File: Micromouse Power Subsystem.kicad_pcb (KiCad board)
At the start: 2 copper layers, 1 part, among them U1 INA219AxDCN

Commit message: Created branch for Josh
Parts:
- added J2: Conn_02x16_Odd_Even, Connector_PinHeader_2.54mm:PinHeader_2x16_P2.54mm_Vertical, F.Cu at (55.9, 63.5)
- added R1: 100m, Resistor_SMD:R_Shunt_Ohmite_LVK12, F.Cu at (62.8, 70.7)
- U1: value INA219AxDCN -> INA219AxD; footprint Package_TO_SOT_SMD:SOT-23-8 -> Package_SO:SOIC-8_3.9x4.9mm_P1.27mm
- moved U1 16.6 mm to (65.0, 64.4)
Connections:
- U1 pad 1: unconnected-(U1-IN+-Pad1) -> /3V3_OUT
- U1 pad 2: unconnected-(U1-IN--Pad2) -> GND
- U1 pad 3: unconnected-(U1-GND-Pad3) -> /SDA
- U1 pad 4: unconnected-(U1-VS-Pad4) -> /SCL
- U1 pad 5: unconnected-(U1-SCL-Pad5) -> /3V3_OUT
- U1 pad 6: unconnected-(U1-SDA-Pad6) -> GND
- U1 pad 7: unconnected-(U1-A0-Pad7) -> GND
- U1 pad 8: unconnected-(U1-A1-Pad8) -> /V_Switch

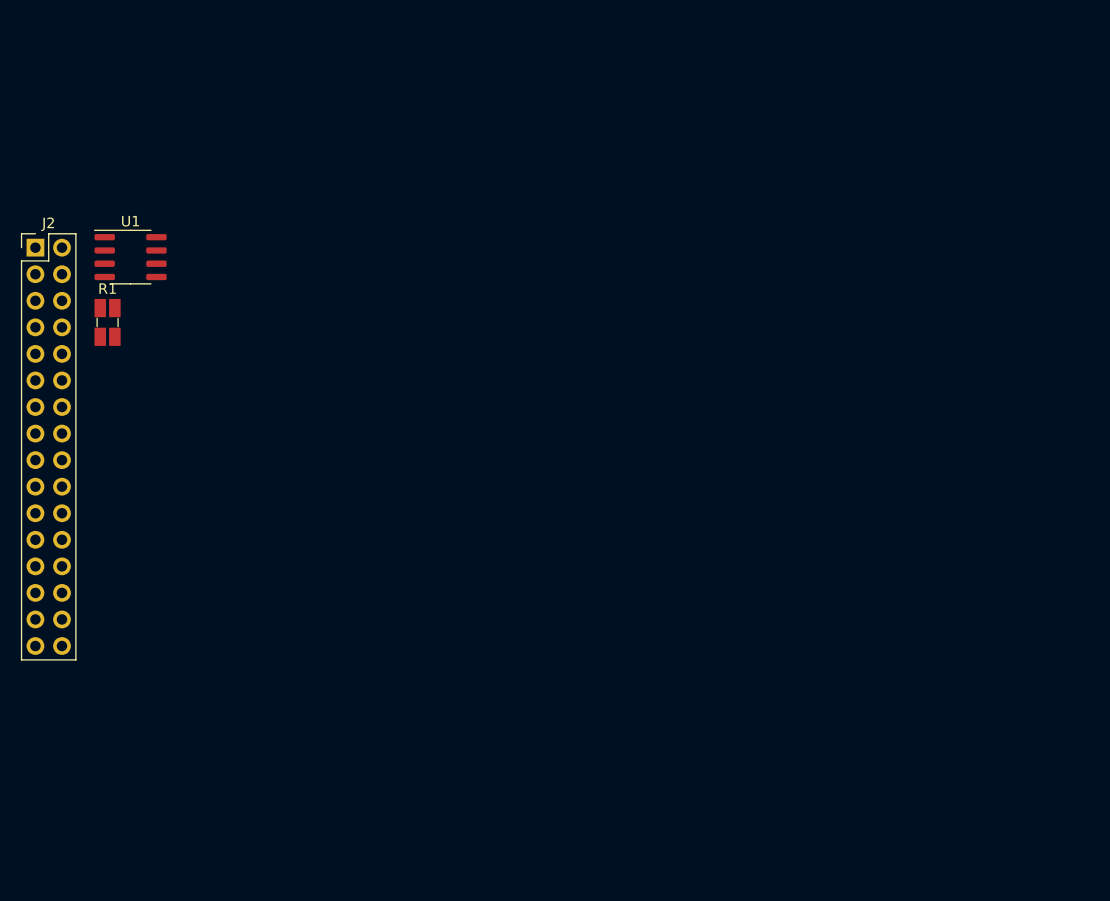
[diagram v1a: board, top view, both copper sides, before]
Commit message: Finished the USB-C integration with PD (9V)
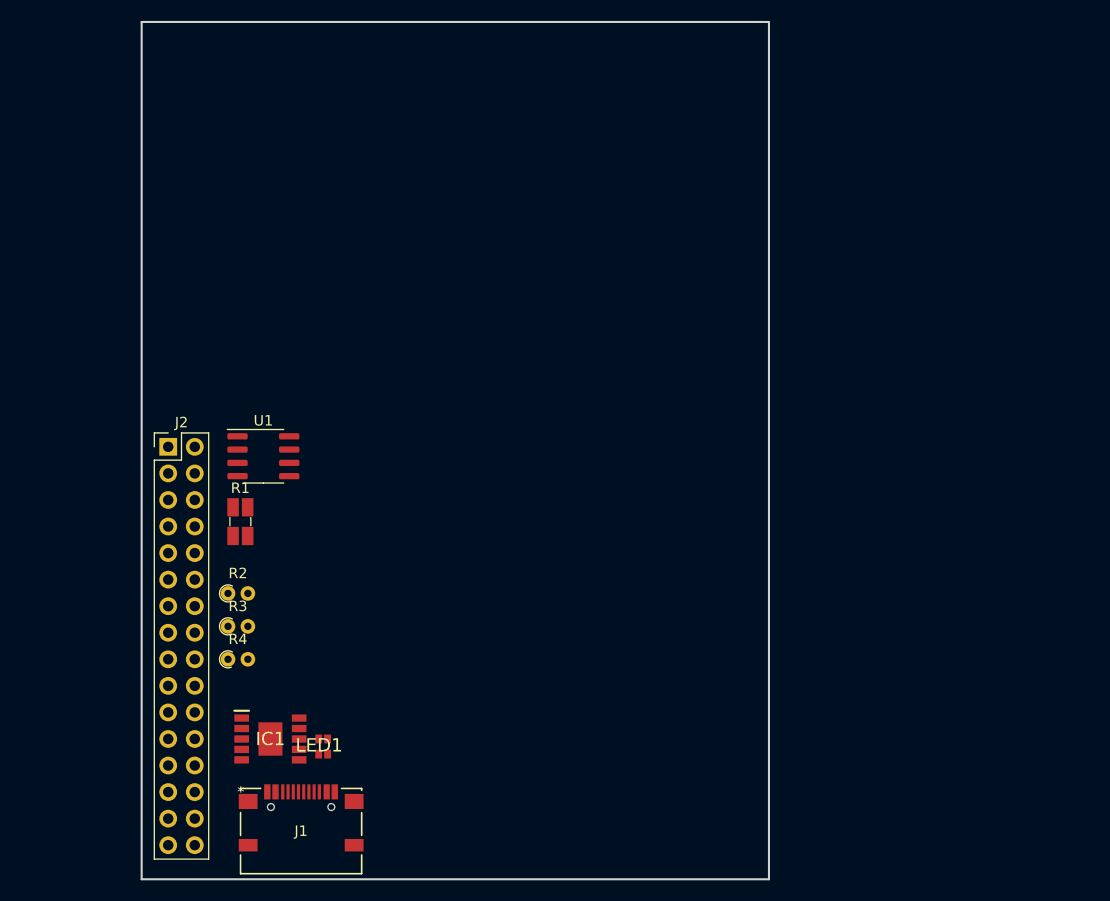
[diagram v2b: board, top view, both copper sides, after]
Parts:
- added IC1: CH224K, Components:SOP100P600X180-11N, F.Cu at (78.4, 110.5)
- added J1: TYPEC-304-ACP16, Components:TYPEC-304-ACP16_XNP, F.Cu at (81.3, 119.3)
- added LED1: LTST-C19HE1WT, RGB LED:LTST-C19HE1WT, F.Cu at (83.4, 111.2)
- added R2: 6.8k, Resistor_THT:R_Axial_DIN0204_L3.6mm_D1.6mm_P1.90mm_Vertical, F.Cu at (74.3, 96.6)
- added R3: 150R, Resistor_THT:R_Axial_DIN0204_L3.6mm_D1.6mm_P1.90mm_Vertical, F.Cu at (74.3, 99.7)
- added R4: 10k, Resistor_THT:R_Axial_DIN0204_L3.6mm_D1.6mm_P1.90mm_Vertical, F.Cu at (74.3, 102.9)
- U1: value INA219AxD -> INA219AIDCNR
- moved R1 22.9 mm to (75.5, 89.7)
- moved U1 22.9 mm to (77.7, 83.5)
- moved J2 22.9 mm to (68.6, 82.5)
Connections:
- J2 pad 1: unconnected-(J2-Pin_1-Pad1) -> /Motor2_B_OUT
- J2 pad 10: unconnected-(J2-Pin_10-Pad10) -> /Motor2_B_OUT
- J2 pad 11: unconnected-(J2-Pin_11-Pad11) -> /EXT_LOAD2_OUT
- J2 pad 12: unconnected-(J2-Pin_12-Pad12) -> /USART2_TX
- J2 pad 13: unconnected-(J2-Pin_13-Pad13) -> /FAST_CHARGE_CTRL
- J2 pad 18: /3V3_OUT -> +3V3
- J2 pad 2: unconnected-(J2-Pin_2-Pad2) -> /Motor2_A_OUT
- J2 pad 20: unconnected-(J2-Pin_20-Pad20) -> +5V
- J2 pad 21: unconnected-(J2-Pin_21-Pad21) -> /EXT_LOAD1_OUT
- J2 pad 22: unconnected-(J2-Pin_22-Pad22) -> /HV
- J2 pad 23: unconnected-(J2-Pin_23-Pad23) -> GND
- J2 pad 24: unconnected-(J2-Pin_24-Pad24) -> /MOTOR3_CTRL1
- J2 pad 25: unconnected-(J2-Pin_25-Pad25) -> /CTRL_EXT_LOAD1
- J2 pad 26: unconnected-(J2-Pin_26-Pad26) -> /MOTOR3_CTRL2
- J2 pad 27: unconnected-(J2-Pin_27-Pad27) -> /MOTOR3_A_OUT
- J2 pad 28: unconnected-(J2-Pin_28-Pad28) -> /MOTOR1_CTRL1
- J2 pad 29: unconnected-(J2-Pin_29-Pad29) -> /MOTOR3_B_OUT
- J2 pad 3: unconnected-(J2-Pin_3-Pad3) -> /Motor4_A_OUT
- J2 pad 30: unconnected-(J2-Pin_30-Pad30) -> /MOTOR1_CTRL2
- J2 pad 31: unconnected-(J2-Pin_31-Pad31) -> /MOTOR1_B_OUT
- J2 pad 32: unconnected-(J2-Pin_32-Pad32) -> /MOTOR1_A_OUT
- J2 pad 4: unconnected-(J2-Pin_4-Pad4) -> /Motor2_CTRL1
- J2 pad 5: unconnected-(J2-Pin_5-Pad5) -> /Motor4_B_OUT
- J2 pad 6: unconnected-(J2-Pin_6-Pad6) -> /Motor2_CTRL2
- J2 pad 7: unconnected-(J2-Pin_7-Pad7) -> /CTRL_EXT_LOAD2
- J2 pad 8: unconnected-(J2-Pin_8-Pad8) -> /Motor4_CTRL1
- J2 pad 9: unconnected-(J2-Pin_9-Pad9) -> /USART2_RX
- R1 pad 2: /V_Switch -> /BAT+
- U1 pad 1: /3V3_OUT -> /BAT+
- U1 pad 3: /SDA -> GND
- U1 pad 4: /SCL -> +3V3
- U1 pad 5: /3V3_OUT -> /SCL
- U1 pad 6: GND -> /SDA
- U1 pad 8: /V_Switch -> +3V3
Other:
- board outline added: 60 x 82 mm

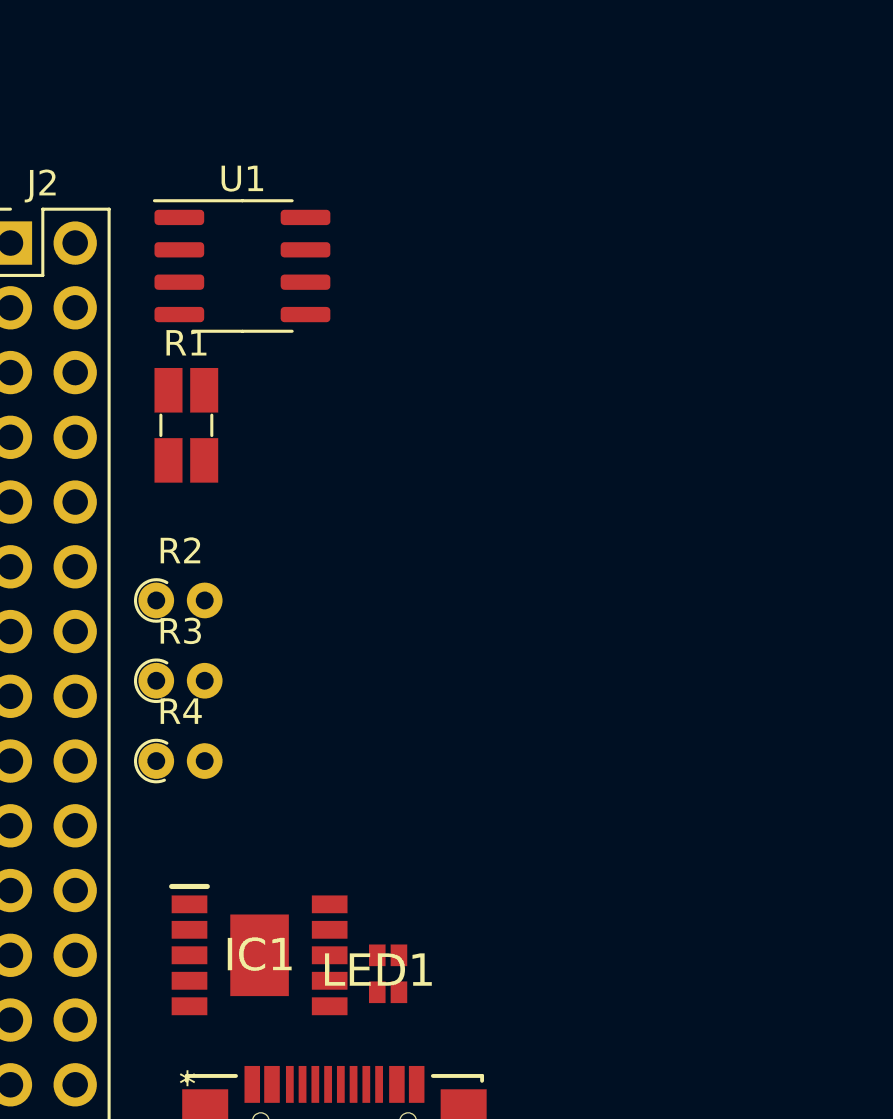
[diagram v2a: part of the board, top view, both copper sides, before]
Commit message: Added the charging modes as well as the charger powering the circuit when plugged in.
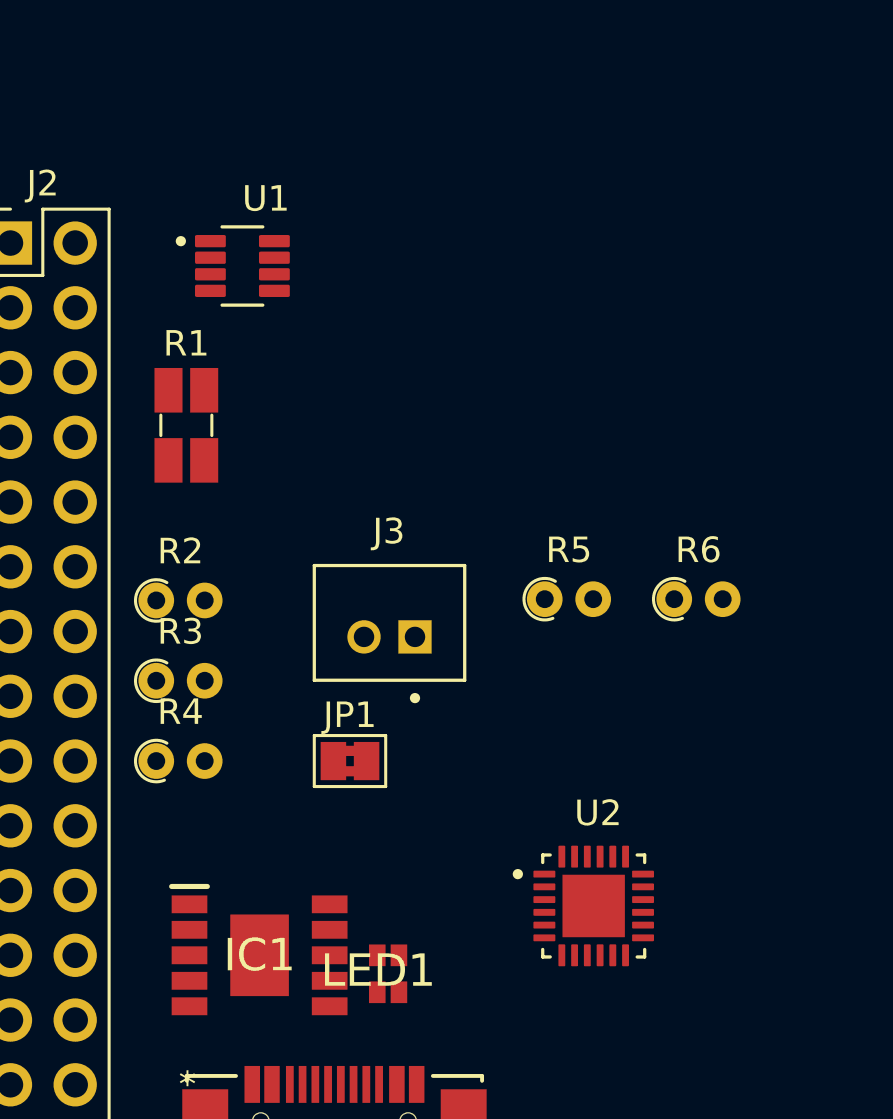
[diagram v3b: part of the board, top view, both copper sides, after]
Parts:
- added J3: B2B-PH-K-S, Battery JST Connector:JST_B2B-PH-K-S, F.Cu at (83.5, 97.5)
- added JP1: Jumper_2_Bridged, Jumper:SolderJumper-2_P1.3mm_Bridged2Bar_Pad1.0x1.5mm, F.Cu at (81.9, 102.9)
- added R5: 10k, Resistor_THT:R_Axial_DIN0204_L3.6mm_D1.6mm_P1.90mm_Vertical, F.Cu at (89.5, 96.5)
- added R6: 10k, Resistor_THT:R_Axial_DIN0204_L3.6mm_D1.6mm_P1.90mm_Vertical, F.Cu at (94.6, 96.5)
- added U2: BQ24610RGER, Battery Charger:QFN50P400X400X100-25N, F.Cu at (91.5, 108.6)
- U1: footprint Package_SO:SOIC-8_3.9x4.9mm_P1.27mm -> INA219:SOT65P280X145-8N

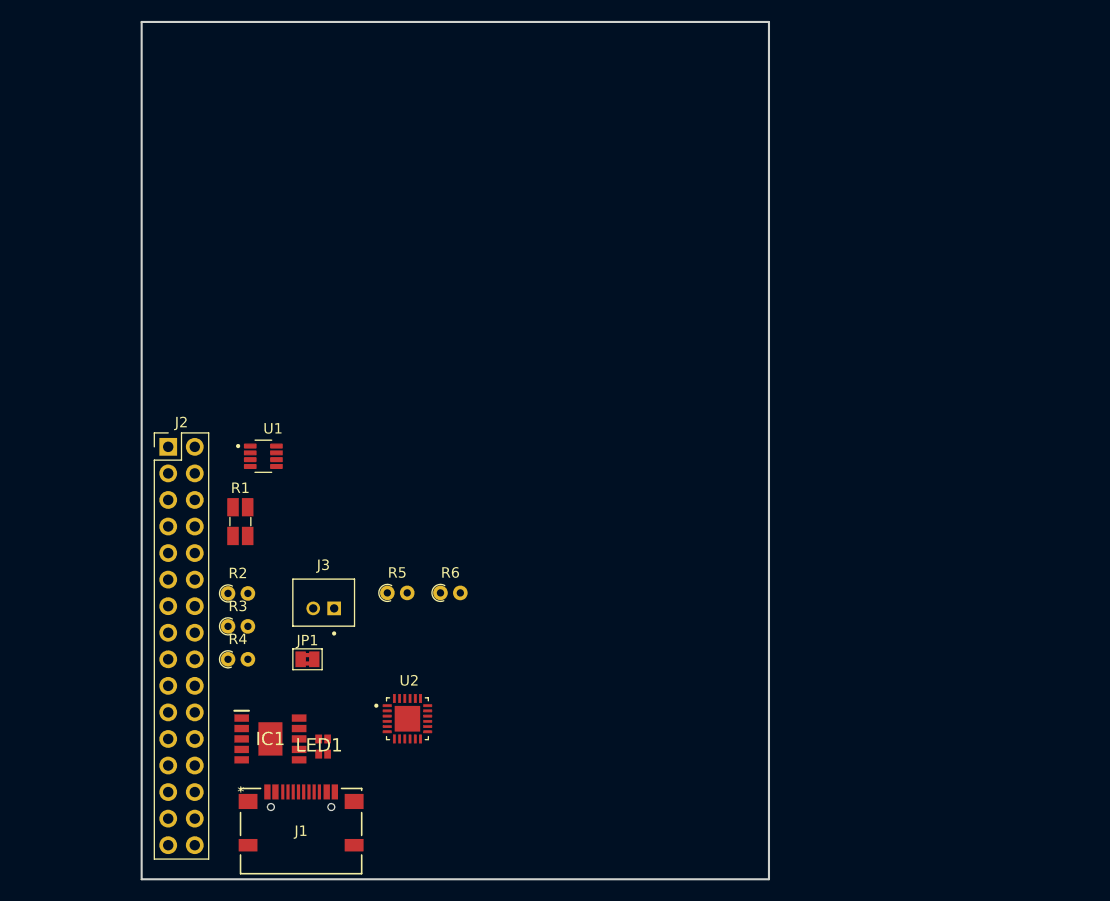
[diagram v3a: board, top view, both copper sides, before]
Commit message: Added completed schematic for my sections
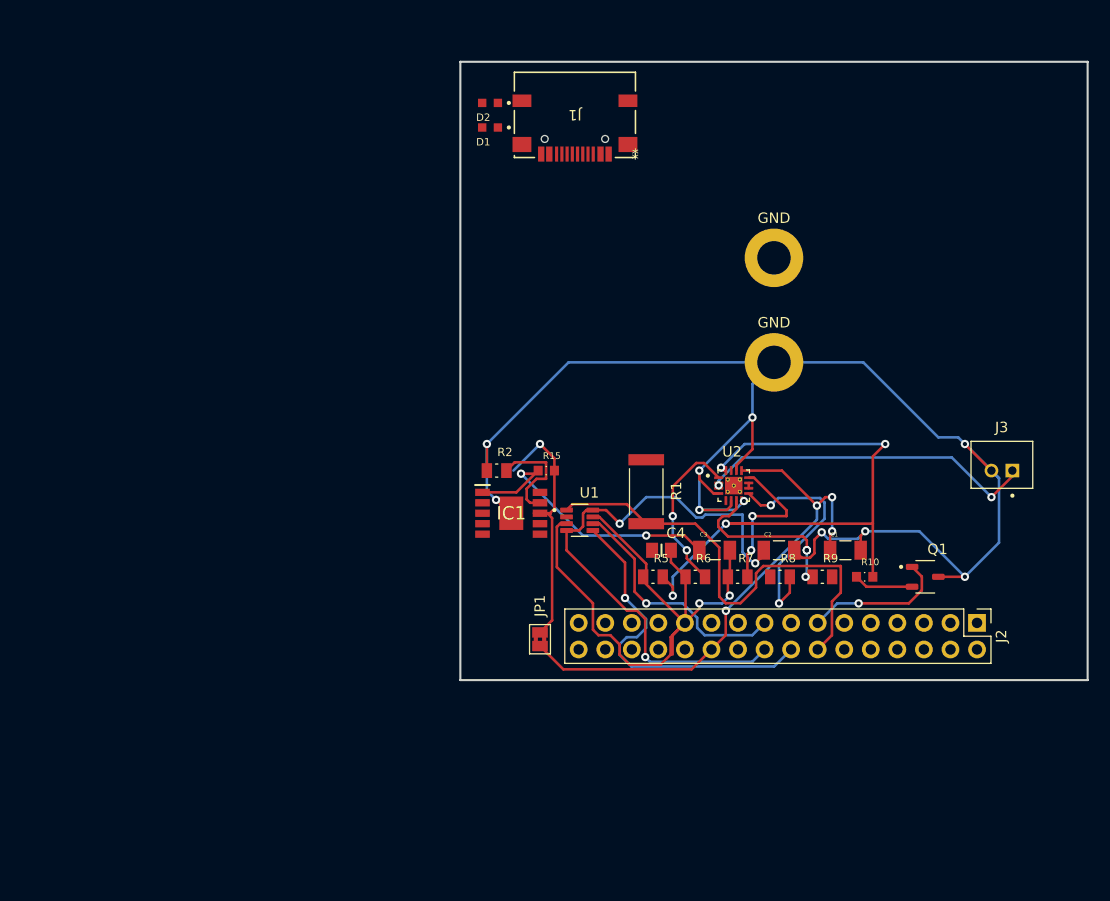
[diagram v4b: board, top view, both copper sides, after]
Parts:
- removed LED1: LTST-C19HE1WT, RGB LED:LTST-C19HE1WT
- removed R3: 150R, Resistor_THT:R_Axial_DIN0204_L3.6mm_D1.6mm_P1.90mm_Vertical
- removed R4: 10k, Resistor_THT:R_Axial_DIN0204_L3.6mm_D1.6mm_P1.90mm_Vertical
- added C1: 1µ, 1 micro:CAPC3216X180N, F.Cu at (133.3, 92.4)
- added C2: 10µ, 10 micro:CAPC3216X180N, F.Cu at (127.0, 92.4)
- added C3: 10µ, 10 micro:CAPC3216X180N, F.Cu at (120.8, 92.4)
- added C4: 4.7µ, 4.7 micro:CAPC2012X140N, F.Cu at (115.8, 92.4)
- added D1: KT-0805G (GREEN), LED:LED_KT-0603R, F.Cu at (99.4, 52.0)
- added D2: KT-0603R (RED), LED:LED_KT-0603R, F.Cu at (99.4, 49.7)
- added GND: MountingHole_3.2mm_M3_DIN965_Pad, MountingHole:MountingHole_3.2mm_M3_DIN965_Pad, F.Cu at (126.5, 64.5)
- added GND: MountingHole_3.2mm_M3_DIN965_Pad, MountingHole:MountingHole_3.2mm_M3_DIN965_Pad, F.Cu at (126.5, 74.5)
- added Q1: AO3400A, MOSFET:SOT95P280X125-3N, F.Cu at (141.0, 95.0)
- added R10: 2.2k, 2.2k:RESC1608X55N, F.Cu at (135.2, 95.0)
- added R15: 200R, 200 ohm:RESC1608X55N, F.Cu at (104.7, 84.8)
- added R7: 1.2k, 1.2k:RESC2012X65N, F.Cu at (123.0, 95.0)
- added R8: 100R, 100 ohm:RESC2012X65N, F.Cu at (127.1, 95.0)
- added R9: 100R, 100 ohm:RESC2012X65N, F.Cu at (131.1, 95.0)
- R1: footprint Resistor_SMD:R_Shunt_Ohmite_LVK12 -> 100m:RESC6332X65N
- R2: footprint Resistor_THT:R_Axial_DIN0204_L3.6mm_D1.6mm_P1.90mm_Vertical -> 6.8k:RESC2012X65N
- R5: value 10k -> 4.7k; footprint Resistor_THT:R_Axial_DIN0204_L3.6mm_D1.6mm_P1.90mm_Vertical -> 4.7k:RESC2012X65N
- R6: footprint Resistor_THT:R_Axial_DIN0204_L3.6mm_D1.6mm_P1.90mm_Vertical -> 10k:RESC2012X65N
- U2: value BQ24610RGER -> BQ24074RGTR; footprint Battery Charger:QFN50P400X400X100-25N -> BQ24074:QFN50P300X300X100-17N
- moved J2 79.2 mm to (145.9, 99.4), turned to -90 degrees
- moved J1 73.3 mm to (107.5, 50.8), turned to 180 degrees
- moved J3 66.2 mm to (148.3, 84.3)
- moved R1 38.9 mm to (114.3, 86.8), turned to -90 degrees
- moved U2 38.4 mm to (122.7, 86.3)
- moved IC1 31.6 mm to (101.4, 88.9)
- moved U1 30.9 mm to (107.9, 89.6)
- moved R2 28.3 mm to (100.0, 84.8)
- moved R5 25.5 mm to (114.9, 95.0)
- moved R6 24.4 mm to (119.0, 95.0)
- moved JP1 22.3 mm to (104.1, 101.0), turned to 90 degrees
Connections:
- IC1 pad 1: unconnected-(IC1-VDD-Pad1) -> Net-(IC1-VDD)
- IC1 pad 10: Net-(IC1-PG) -> unconnected-(IC1-PG-Pad10)
- J1 pad B1-A12: unconnected-(J1-VBUS-PadB1-A12) -> GND
- J1 pad B4-A9: GND -> unconnected-(J1-VBUS-PadB4-A9)
- J3 pad 1: Net-(J3-Pad1) -> Net-(U2-BAT_2)
- R1 pad 1: GND -> /SYS
- R5 pad 1: Net-(U2-VFB) -> GND
- R5 pad 2: GND -> Net-(U2-ISET)
- R6 pad 1: Net-(J3-Pad1) -> GND
- R6 pad 2: Net-(U2-VFB) -> Net-(U2-TS)
- U1 pad 2: GND -> /SYS
- U2 pad 1: unconnected-(U2-ACN-Pad1) -> Net-(U2-TS)
- U2 pad 10: unconnected-(U2-VREF-Pad10) -> /SYS
- U2 pad 11: unconnected-(U2-ISET1-Pad11) -> /SYS
- U2 pad 12: Net-(U2-VFB) -> Net-(U2-ILIM)
- U2 pad 13: unconnected-(U2-SRN-Pad13) -> /HV
- U2 pad 14: unconnected-(U2-SRP-Pad14) -> GND
- U2 pad 16: unconnected-(U2-ACSET-Pad16) -> Net-(U2-ISET)
- U2 pad 18: unconnected-(U2-REGN-Pad18) -> (no net)
- U2 pad 19: unconnected-(U2-LODRV-Pad19) -> (no net)
- U2 pad 2: unconnected-(U2-ACP-Pad2) -> Net-(U2-BAT_2)
- U2 pad 20: unconnected-(U2-PH-Pad20) -> (no net)
- U2 pad 21: unconnected-(U2-HIDRV-Pad21) -> (no net)
- U2 pad 22: unconnected-(U2-BTST-Pad22) -> (no net)
- U2 pad 3: unconnected-(U2-~{ACDRV}-Pad3) -> Net-(U2-BAT_2)
- U2 pad 4: unconnected-(U2-CE-Pad4) -> GND
- U2 pad 5: unconnected-(U2-STAT1-Pad5) -> /SYS
- U2 pad 6: unconnected-(U2-TS-Pad6) -> GND
- U2 pad 7: unconnected-(U2-TTC-Pad7) -> Net-(U2-~{PGOOD})
- U2 pad 8: unconnected-(U2-~{PG}-Pad8) -> GND
- U2 pad 9: unconnected-(U2-STAT2-Pad9) -> Net-(U2-~{CHG})
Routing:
- net GND: track 0.00 -> 203.8 mm, vias 0 -> 12
- net Net-(U2-ISET): track 0.00 -> 58.2 mm, vias 0 -> 4
- net +3V3: track 0.00 -> 55.6 mm, vias 0 -> 3
- net /HV: track 0.00 -> 51.6 mm, vias 0 -> 4
- net /BAT+: track 0.00 -> 44.3 mm
- net /SCL: track 0.00 -> 33.2 mm, vias 0 -> 1
- net Net-(U2-BAT_2): track 0.00 -> 33.1 mm, vias 0 -> 2
- net Net-(IC1-VDD): track 0.00 -> 28.0 mm, vias 0 -> 2
- net /VBUS: track 0.00 -> 25.4 mm, vias 0 -> 1
- net /SDA: track 0.00 -> 23.7 mm, vias 0 -> 1
- net Net-(U2-~{CHG}): track 0.00 -> 22.6 mm, vias 0 -> 2
- net Net-(U2-~{PGOOD}): track 0.00 -> 16.9 mm, vias 0 -> 3
- net Net-(U2-TS): track 0.00 -> 15.8 mm, vias 0 -> 2
- net Net-(U2-ILIM): track 0.00 -> 14.8 mm, vias 0 -> 2
- net /FAST_CHARGE_CTRL: track 0.00 -> 13.9 mm, vias 0 -> 1
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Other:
- board size 60 x 82 mm -> 60 x 59.1 mm
